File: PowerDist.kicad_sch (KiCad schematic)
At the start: 17 parts, among them J18 PowerConn, Q2 CSD18511KTT, U12 RI3-1205S, U13 NCP1117-3.3_SOT223

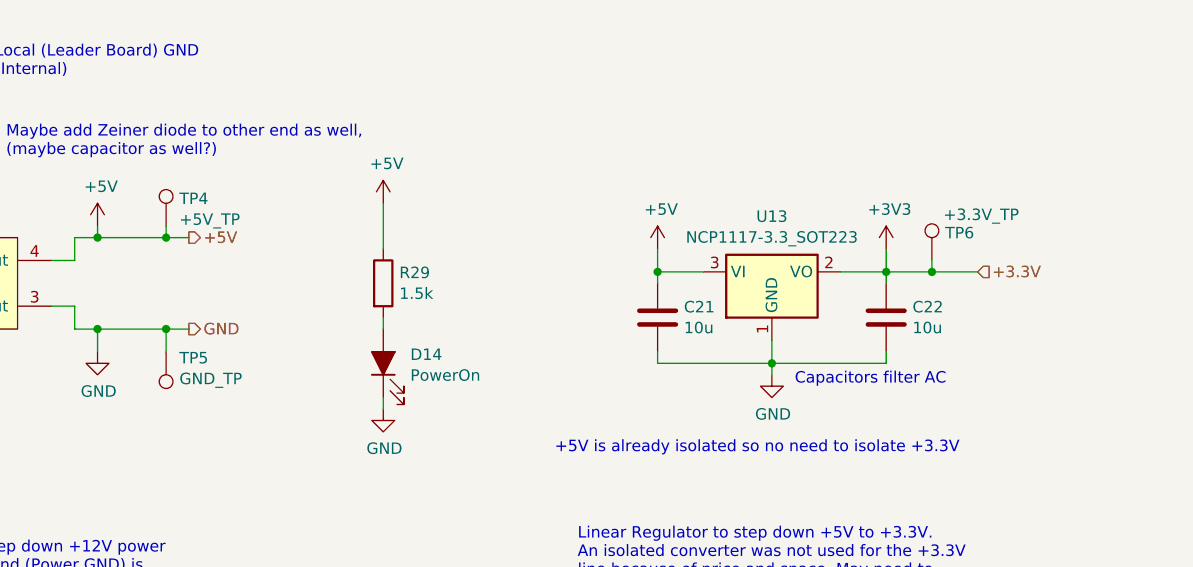
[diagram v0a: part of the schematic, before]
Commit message: Started cleaning some comments, changed EL3H7 data sheet link, removed extra motor CAN connector and changed original one to match (I think) motor controller connector, removed extra mounting holes, removed hierarchical power labels.
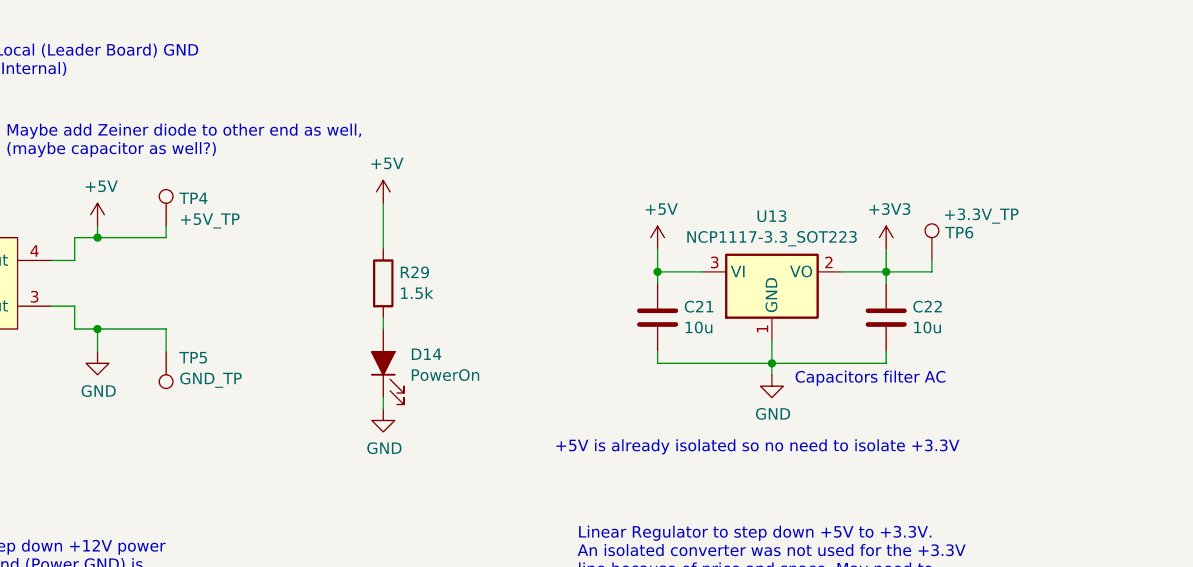
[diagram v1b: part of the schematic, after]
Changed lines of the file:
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@@
-	)
-	(junction
-		(at 222.25 81.28)
-		(diameter 0)
-		(color 0 0 0 0)
 	)
 	(junction
@@
 	)
 	(junction
-		(at 137.16 77.47)
-		(diameter 0)
-		(color 0 0 0 0)
-	)
-	(junction
 		(at 129.54 87.63)
 		(diameter 0)
@@
 	)
 	(junction
-		(at 137.16 87.63)
-		(diameter 0)
-		(color 0 0 0 0)
-	)
-	(junction
 		(at 217.17 81.28)
 		(diameter 0)
@@
 	(wire
 		(pts
-			(xy 227.33 81.28) (xy 222.25 81.28)
-		)
-		(stroke
-			(width 0)
-			(type default)
-		)
-	)
-	(wire
-		(pts
 			(xy 191.77 81.28) (xy 191.77 82.55)
 		)
@@
 	(wire
 		(pts
-			(xy 137.16 77.47) (xy 139.7 77.47)
-		)
-		(stroke
-			(width 0)
-			(type default)
-		)
-	)
-	(wire
-		(pts
 			(xy 49.53 81.28) (xy 43.18 81.28)
 		)
@@
 		(pts
 			(xy 99.06 85.09) (xy 101.6 85.09)
-		)
-		(stroke
-			(width 0)
-			(type default)
-		)
-	)
-	(wire
-		(pts
-			(xy 139.7 87.63) (xy 137.16 87.63)
 		)
 		(stroke
@@
 		)
 	)
-	(hierarchical_label "+3.3V"
-		(shape input)
-		(at 227.33 81.28 0)
-		(fields_autoplaced yes)
-		(effects
-			(font
-				(size 1.27 1.27)
-			)
-			(justify left)
-		)
-	)
-	(hierarchical_label "GND"
-		(shape output)
-		(at 139.7 87.63 0)
-		(fields_autoplaced yes)
-		(effects
-			(font
-				(size 1.27 1.27)
-			)
-			(justify left)
-		)
-	)
-	(hierarchical_label "+5V"
-		(shape output)
-		(at 139.7 77.47 0)
-		(fields_autoplaced yes)
-		(effects
-			(font
-				(size 1.27 1.27)
-			)
-			(justify left)
-		)
-	)

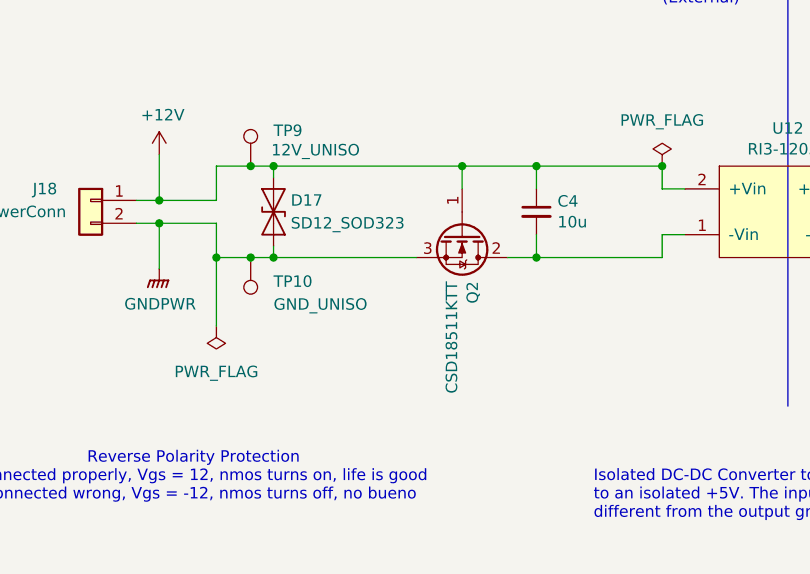
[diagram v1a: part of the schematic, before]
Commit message: renamed power state indicators to contactors and removed unused contactors, added current limiting resistors to lights drivers, changed mosfet to new mosfet
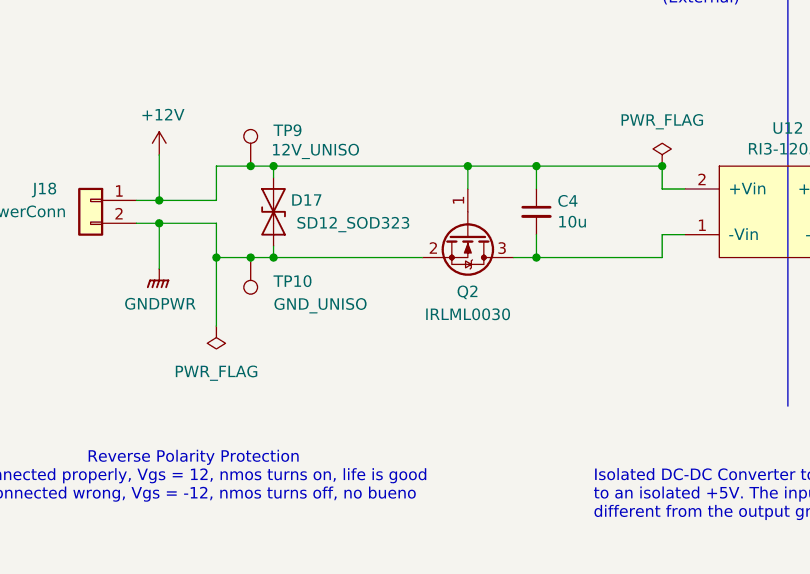
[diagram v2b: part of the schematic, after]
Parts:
- removed Q2: CSD18511KTT, Package_TO_SOT_SMD:TO-252-2, symbol Device:Q_NMOS_GDS
- added Q2: IRLML0030, Package_TO_SOT_SMD:SOT-23, symbol Transistor_FET:IRLML0030
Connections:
- net +12V: now also Q2.1 (G)
- net GNDPWR: now also Q2.2 (S)
- net at C4.2, U12.1 (-Vin): now also Q2.3 (D)

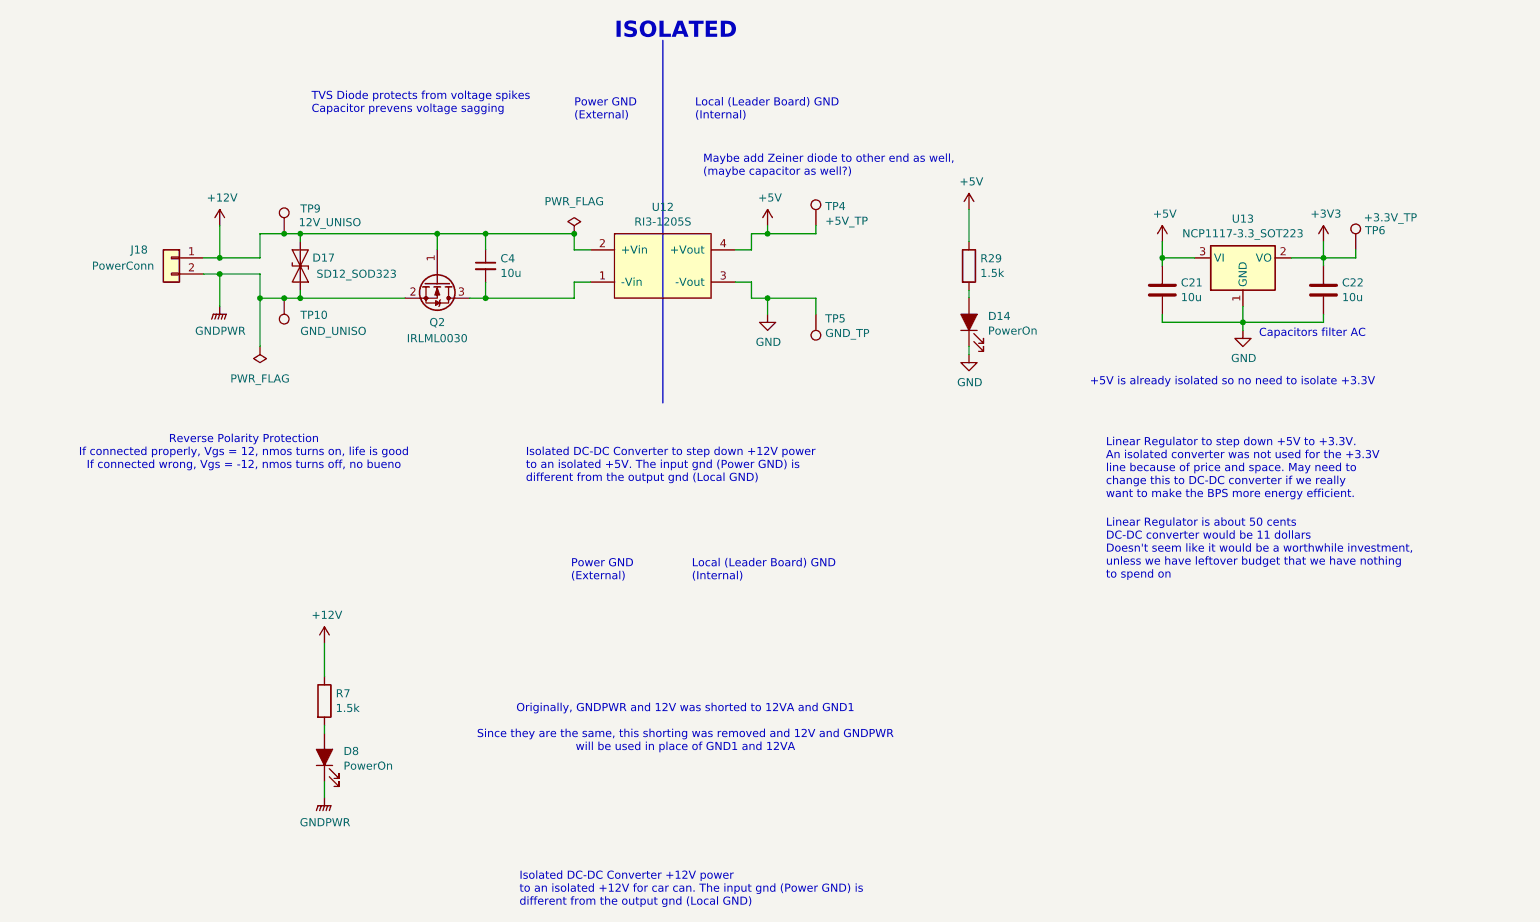
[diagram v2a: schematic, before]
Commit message: added circuitry for limit switch brake, added mosfet to drive LEDs, cleaned up legacy comments, updated resistor values for LEDs
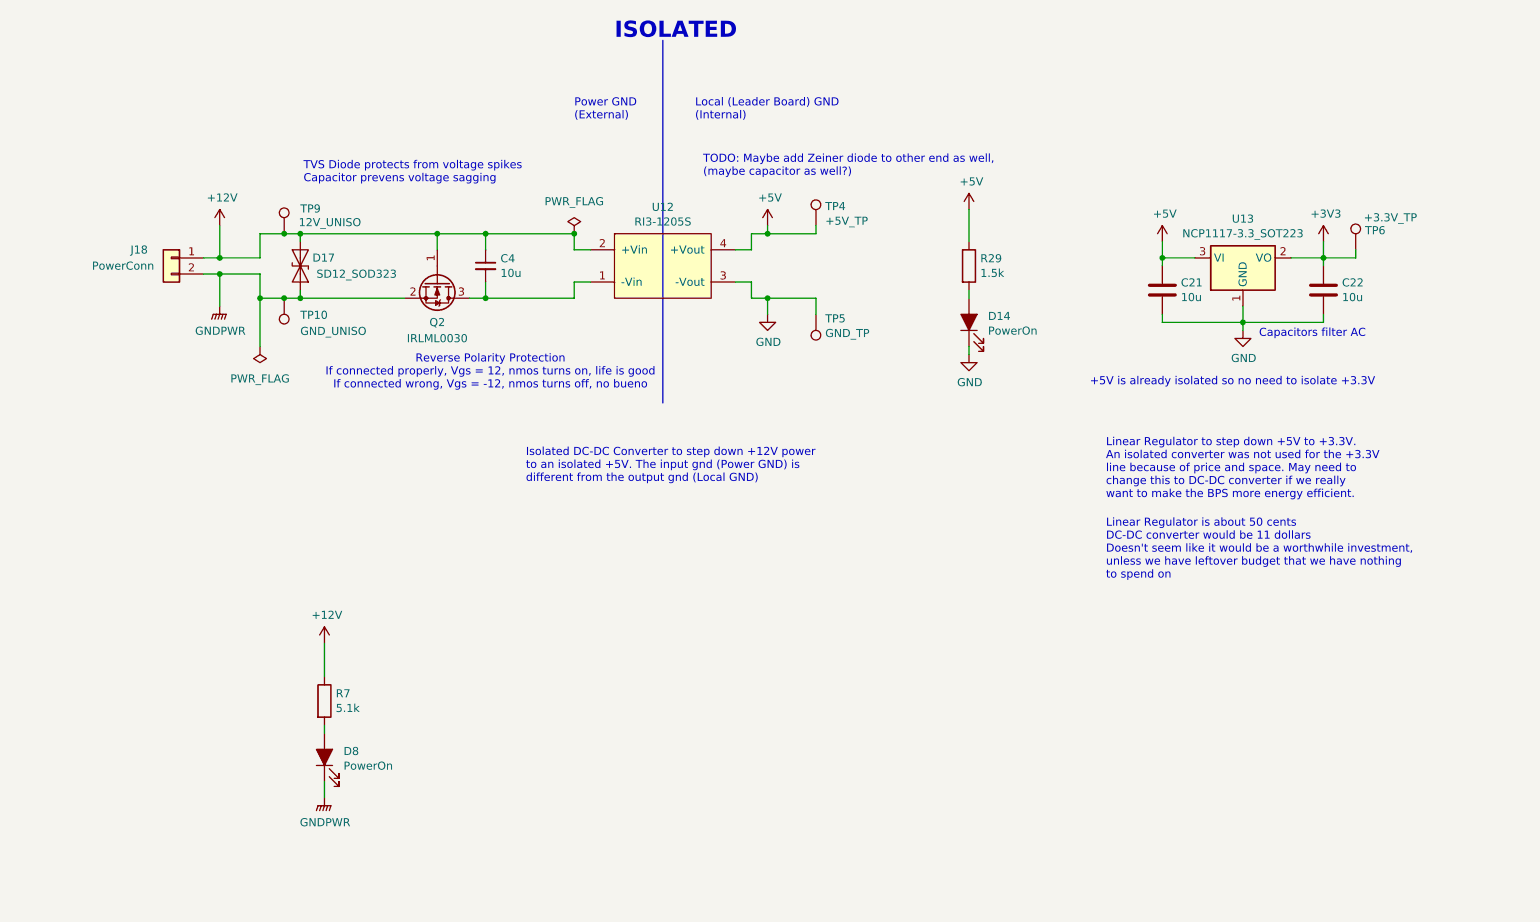
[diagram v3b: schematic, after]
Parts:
- R7: value 1.5k -> 5.1k
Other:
- note added: "TODO: Maybe add Zeiner diode to other end as well, (maybe capacitor as well?)"
- note removed: "Isolated DC-DC Converter +12V power to an isolated +12V for car can. The input gnd (Power GND) is different from the output gnd (Local GND)"
- note removed: "Maybe add Zeiner diode to other end as well, (maybe capacitor as well?)"
- note removed: "Originally, GNDPWR and 12V was shorted to 12VA and GND1 Since they are the same, this shorting was removed and 12V and GNDPWR will be used in place of GND1 and 12VA"
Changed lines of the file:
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@@
-		)
-	)
-	(text "Power GND\n(External)"
-		(exclude_from_sim no)
-		(at 98.552 132.334 0)
-		(effects
-			(font
-				(size 1.27 1.27)
-			)
-			(justify left bottom)
-		)
-	)
-	(text "Local (Leader Board) GND\n(Internal)"
-		(exclude_from_sim no)
-		(at 117.602 132.334 0)
-		(effects
-			(font
-				(size 1.27 1.27)
-			)
-			(justify left bottom)
 		)
 	)
@@
 		)
 	)
-	(text "Maybe add Zeiner diode to other end as well,\n(maybe capacitor as well?)"
+	(text "TODO: Maybe add Zeiner diode to other end as well,\n(maybe capacitor as well?)"
 		(exclude_from_sim no)
 		(at 119.38 68.58 0)
@@
 				(size 1.27 1.27)
 				(color 255 17 10 1)
-			)
-			(justify left bottom)
-		)
-	)
-	(text "Isolated DC-DC Converter +12V power\nto an isolated +12V for car can. The input gnd (Power GND) is\ndifferent from the output gnd (Local GND)"
-		(exclude_from_sim no)
-		(at 90.424 183.642 0)
-		(effects
-			(font
-				(size 1.27 1.27)
 			)
 			(justify left bottom)
@@
 	(text "TVS Diode protects from voltage spikes\nCapacitor prevens voltage sagging\n"
 		(exclude_from_sim no)
-		(at 57.658 58.674 0)
+		(at 56.388 69.596 0)
 		(effects
 			(font
@@
 			)
 			(justify left bottom)
-		)
-	)
-	(text "Originally, GNDPWR and 12V was shorted to 12VA and GND1\n\nSince they are the same, this shorting was removed and 12V and GNDPWR\nwill be used in place of GND1 and 12VA\n"
-		(exclude_from_sim no)
-		(at 116.586 155.448 0)
-		(effects
-			(font
-				(size 1.27 1.27)
-				(color 255 16 12 1)
-			)
 		)
 	)
@@
 	(text "Reverse Polarity Protection\nIf connected properly, Vgs = 12, nmos turns on, life is good\nIf connected wrong, Vgs = -12, nmos turns off, no bueno"
 		(exclude_from_sim no)
-		(at 46.99 112.014 0)
+		(at 85.852 99.314 0)
 		(effects
 			(font
@@
 			)
 		)
-		(property "Value" "1.5k"
+		(property "Value" "5.1k"
 			(at 61.468 152.273 0)
 			(effects

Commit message: fixed some footprints and part numbers
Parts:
- C21, C22: Mouser Part Number (none) -> 963-TMK212BBJ106MGHT
- C4: Mouser Part Number (none) -> 963-TMK212BBJ106MGHT; P/N C0805C105K3PACTU -> (none)
- D14, D8: Mouser Part Number (none) -> 604-APTD2012LCGCK
- D17: Mouser Part Number (none) -> 863-NSVR0320MW2T1G
- Q2: Mouser Part Number (none) -> 771-BUK9M23-80EX
- R29: Mouser Part Number (none) -> 71-CRCW08051K50JNEB
- R7: P/N (none) -> Inventory
- U13: Mouser Part Number (none) -> 863-NCP1117ST33T3G
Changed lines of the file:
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@@
+			)
+		)
+		(property "Mouser Part Number" "604-APTD2012LCGCK"
+			(at 161.29 91.44 0)
+			(effects
+				(font
+					(size 1.27 1.27)
+				)
+				(hide yes)
 			)
 		)
@@
 			)
 		)
+		(property "Mouser Part Number" "71-CRCW08051K50JNEB"
+			(at 161.29 82.55 0)
+			(effects
+				(font
+					(size 1.27 1.27)
+				)
+				(hide yes)
+			)
+		)
 		(pin "1"
 		)
@@
 			)
 		)
+		(property "Mouser Part Number" "863-NCP1117ST33T3G"
+			(at 204.47 81.28 0)
+			(effects
+				(font
+					(size 1.27 1.27)
+				)
+				(hide yes)
+			)
+		)
 		(pin "1"
 		)
@@
 			)
 		)
+		(property "Mouser Part Number" "963-TMK212BBJ106MGHT"
+			(at 191.77 86.36 0)
+			(effects
+				(font
+					(size 1.27 1.27)
+				)
+				(hide yes)
+			)
+		)
 		(pin "1"
 		)
@@
 		)
 		(property "Vds" ""
+			(at 217.17 86.36 0)
+			(effects
+				(font
+					(size 1.27 1.27)
+				)
+				(hide yes)
+			)
+		)
+		(property "Mouser Part Number" "963-TMK212BBJ106MGHT"
 			(at 217.17 86.36 0)
 			(effects
@@
 			)
 		)
+		(property "Mouser Part Number" "604-APTD2012LCGCK"
+			(at 59.69 160.02 0)
+			(effects
+				(font
+					(size 1.27 1.27)
+				)
+				(hide yes)
+			)
+		)
 		(pin "1"
 		)
@@
 		)
 		(property "Vds" ""
+			(at 59.69 151.13 0)
+			(effects
+				(font
+					(size 1.27 1.27)
+				)
+				(hide yes)
+			)
+		)
+		(property "P/N" "Inventory"
 			(at 59.69 151.13 0)
 			(effects
@@
 			)
 		)
+		(property "Mouser Part Number" "771-BUK9M23-80EX"
+			(at 77.47 85.09 0)
+			(effects
+				(font
+					(size 1.27 1.27)
+				)
+				(hide yes)
+			)
+		)
 		(pin "2"
 		)
@@
 			)
 		)
+		(property "Mouser Part Number" "863-NSVR0320MW2T1G"
+			(at 55.88 82.55 0)
+			(effects
+				(font
+					(size 1.27 1.27)
+				)
+				(hide yes)
+			)
+		)
 		(pin "1"
 		)
@@
 			)
 		)
-		(property "P/N" "C0805C105K3PACTU"
+		(property "P/N" ""
 			(at 85.09 82.55 0)
 			(effects
@@
 			(at 85.09 82.55 0)
 			(effects
+				(font
+					(size 1.27 1.27)
+				)
+				(hide yes)
+			)
+		)
+		(property "Mouser Part Number" "963-TMK212BBJ106MGHT"
+			(at 85.09 82.55 0)
+			(effects

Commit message: Added/checked datasheet links/part numbers, deleted accel_pot2 and brake_pot2 hierarchical labels and changed corresponding pins (PC2, PC3) to GPIO on the now-2x5 extra GPIO connector.
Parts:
- Q2: Mouser Part Number 771-BUK9M23-80EX -> (none); P/N (none) -> IRLML0030TRPBF
- U12: Mouser Part Number (none) -> 919-RI3-1205S
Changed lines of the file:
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@@
 			)
 		)
-		(property "Datasheet" ""
+		(property "Datasheet" "chrome-extension://efaidnbmnnnibpcajpcglclefindmkaj/https://www.mouser.com/datasheet/2/468/RI3-1711119.pdf"
 			(at 113.03 77.47 0)
 			(effects
@@
 			)
 		)
+		(property "Mouser Part Number" "919-RI3-1205S"
+			(at 113.03 77.47 0)
+			(effects
+				(font
+					(size 1.27 1.27)
+				)
+				(hide yes)
+			)
+		)
 		(pin "1"
 		)
@@
 			)
 		)
-		(property "Datasheet" "~"
+		(property "Datasheet" "https://www.mouser.com/ProductDetail/Kingbright/APTD2012LCGCK?qs=AQlKX63v8RvNHN%2F9EGvNTg%3D%3D&srsltid=AfmBOooAHKD1ehETHFyXma0dZSsRO3OtCs7cgmDquFx90LgeUyiA_vS_"
 			(at 161.29 91.44 0)
 			(effects
@@
 			)
 		)
-		(property "Datasheet" "~"
+		(property "Datasheet" "https://www.mouser.com/ProductDetail/Vishay-Dale/CRCW08051K50JNEB?qs=1CkV0QOCgMrzFJsYQ4Ra6w%3D%3D"
 			(at 161.29 82.55 0)
 			(effects
@@
 			)
 		)
-		(property "Datasheet" "~"
+		(property "Datasheet" "https://www.mouser.com/ProductDetail/TAIYO-YUDEN/TMK212BBJ106MGHT?qs=sBf%2Fb4nBSlfab8x4Ir6OCA%3D%3D&srsltid=AfmBOoryff5Ub5fZJJeEGNmqKnKu_K1PXKxJXyecjVGIa794GPQPVrnJ"
 			(at 191.77 86.36 0)
 			(effects
@@
 			)
 		)
-		(property "Datasheet" "~"
+		(property "Datasheet" "https://www.mouser.com/ProductDetail/TAIYO-YUDEN/TMK212BBJ106MGHT?qs=sBf%2Fb4nBSlfab8x4Ir6OCA%3D%3D&srsltid=AfmBOoryff5Ub5fZJJeEGNmqKnKu_K1PXKxJXyecjVGIa794GPQPVrnJ"
 			(at 217.17 86.36 0)
 			(effects
@@
 			)
 		)
-		(property "Datasheet" "~"
+		(property "Datasheet" "https://www.mouser.com/ProductDetail/Kingbright/APTD2012LCGCK?qs=AQlKX63v8RvNHN%2F9EGvNTg%3D%3D&srsltid=AfmBOooAHKD1ehETHFyXma0dZSsRO3OtCs7cgmDquFx90LgeUyiA_vS_"
 			(at 59.69 160.02 0)
 			(effects
@@
 			)
 		)
-		(property "Mouser Part Number" "771-BUK9M23-80EX"
+		(property "Mouser Part Number" ""
+			(at 77.47 85.09 0)
+			(effects
+				(font
+					(size 1.27 1.27)
+				)
+				(hide yes)
+			)
+		)
+		(property "P/N" "  IRLML0030TRPBF"
 			(at 77.47 85.09 0)
 			(effects
@@
 			)
 		)
-		(property "Datasheet" "https://connect.kemet.com:7667/gateway/IntelliData-ComponentDocumentation/1.0/download/specsheet/C0805C105K3PACTU"
+		(property "Datasheet" "https://www.mouser.com/ProductDetail/TAIYO-YUDEN/TMK212BBJ106MGHT?qs=sBf%2Fb4nBSlfab8x4Ir6OCA%3D%3D&srsltid=AfmBOoryff5Ub5fZJJeEGNmqKnKu_K1PXKxJXyecjVGIa794GPQPVrnJ"
 			(at 85.09 82.55 0)
 			(effects

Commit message: Moved some things inward and squished board, added some labels, broke some traces up (sorry Krish 😣)
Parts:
- TP4, TP5, TP6: footprint TestPoint:TestPoint_Pad_1.5x1.5mm -> TestPoint:TestPoint_Keystone_5005-5009_Compact
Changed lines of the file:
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@@
 			)
 		)
-		(property "Footprint" "TestPoint:TestPoint_Pad_1.5x1.5mm"
+		(property "Footprint" "TestPoint:TestPoint_Keystone_5005-5009_Compact"
 			(at 142.24 76.2 0)
 			(effects
@@
 			)
 		)
-		(property "Footprint" "TestPoint:TestPoint_Pad_1.5x1.5mm"
+		(property "Footprint" "TestPoint:TestPoint_Keystone_5005-5009_Compact"
 			(at 132.08 90.17 0)
 			(effects
@@
 			)
 		)
-		(property "Footprint" "TestPoint:TestPoint_Pad_1.5x1.5mm"
+		(property "Footprint" "TestPoint:TestPoint_Keystone_5005-5009_Compact"
 			(at 227.33 80.01 0)
 			(effects
